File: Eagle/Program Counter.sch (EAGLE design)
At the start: 6 parts, among them J1 55959-2430

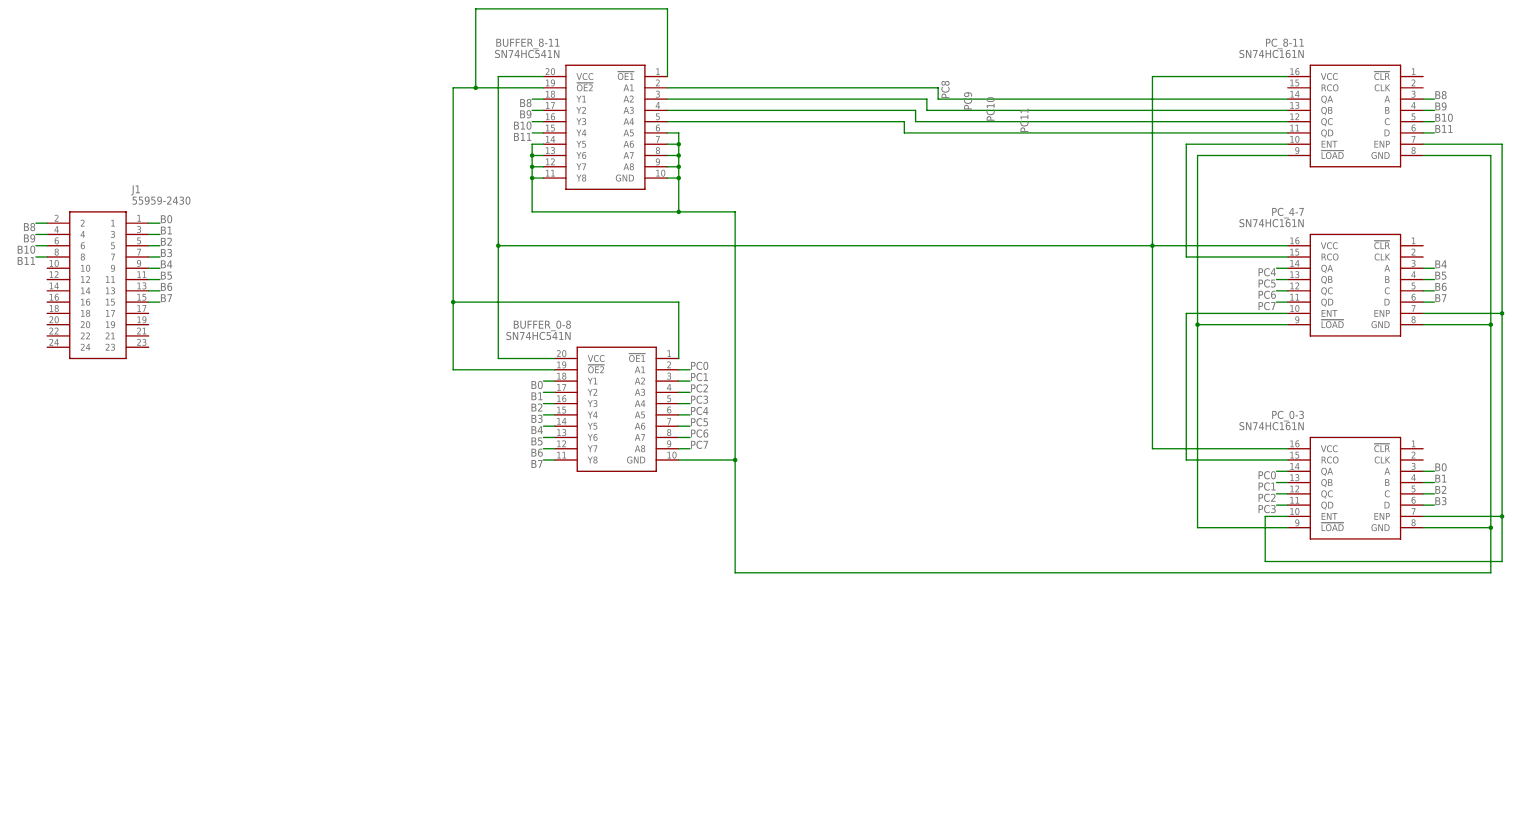
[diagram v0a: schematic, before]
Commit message: finished implementing Program Counter
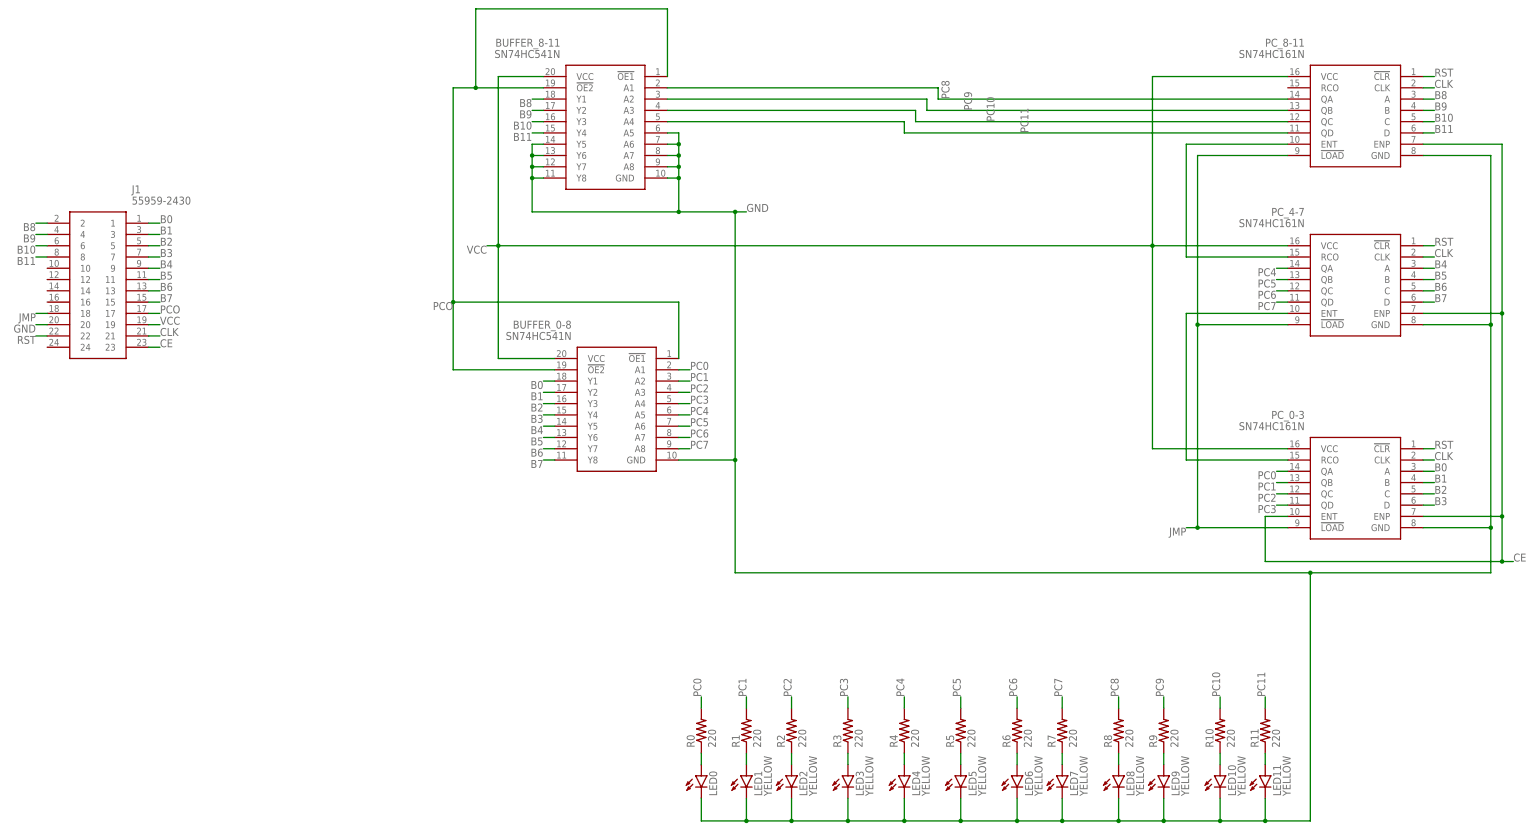
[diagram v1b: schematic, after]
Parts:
- added LED0: (no value), led:LED3MM
- added LED1, LED10, LED11, LED2, LED3, LED4, LED5, LED6, LED7, LED8, LED9: YELLOW, led:LED3MM
- added R0, R1, R10, R11, R2, R3, R4, R5, R6, R7, R8, R9: 220, rcl:R-US_0204/7
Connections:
- removed net N$1: BUFFER_0-8.GND, BUFFER_8-11.A5, BUFFER_8-11.A6, BUFFER_8-11.A7, BUFFER_8-11.A8, BUFFER_8-11.GND, BUFFER_8-11.Y5, BUFFER_8-11.Y6, BUFFER_8-11.Y7, BUFFER_8-11.Y8, PC_0-3.GND, PC_4-7.GND, PC_8-11.GND
- removed net N$4: BUFFER_0-8.!OE1, BUFFER_0-8.!OE2, BUFFER_8-11.!OE1, BUFFER_8-11.!OE2
- removed net N$8: BUFFER_0-8.VCC, BUFFER_8-11.VCC, PC_0-3.VCC, PC_4-7.VCC, PC_8-11.VCC
- new net CE: J1.23, PC_0-3.ENP, PC_0-3.ENT, PC_4-7.ENP, PC_8-11.ENP
- new net CLK: J1.21, PC_0-3.CLK, PC_4-7.CLK, PC_8-11.CLK
- new net GND: BUFFER_0-8.GND, BUFFER_8-11.A5, BUFFER_8-11.A6, BUFFER_8-11.A7, BUFFER_8-11.A8, BUFFER_8-11.GND, BUFFER_8-11.Y5, BUFFER_8-11.Y6, BUFFER_8-11.Y7, BUFFER_8-11.Y8, J1.20, LED0.C, LED1.C, LED10.C, LED11.C, LED2.C, LED3.C, LED4.C, LED5.C, LED6.C, LED7.C, LED8.C, LED9.C, PC_0-3.GND, PC_4-7.GND, PC_8-11.GND
- new net JMP: J1.18, PC_0-3.!LOAD, PC_4-7.!LOAD, PC_8-11.!LOAD
- new net N$10: LED4.A, R4.1
- new net N$11: LED5.A, R5.1
- new net N$12: LED6.A, R6.1
- new net N$13: LED7.A, R7.1
- new net N$14: LED8.A, R8.1
- new net N$15: LED9.A, R9.1
- new net N$16: LED10.A, R10.1
- new net N$17: LED11.A, R11.1
- new net N$7: LED2.A, R2.1
- new net N$9: LED3.A, R3.1
- new net PCO: BUFFER_0-8.!OE1, BUFFER_0-8.!OE2, BUFFER_8-11.!OE1, BUFFER_8-11.!OE2, J1.17
- new net RST: J1.22, PC_0-3.!CLR, PC_4-7.!CLR, PC_8-11.!CLR
- new net VCC: BUFFER_0-8.VCC, BUFFER_8-11.VCC, J1.19, PC_0-3.VCC, PC_4-7.VCC, PC_8-11.VCC
- net N$5: now also LED0.A, R0.1; no longer PC_0-3.!LOAD, PC_4-7.!LOAD, PC_8-11.!LOAD
- net N$6: now also LED1.A, R1.1; no longer PC_0-3.ENP, PC_0-3.ENT, PC_4-7.ENP, PC_8-11.ENP
- net PC0: now also R0.2
- net PC1: now also R1.2
- net PC10: now also R10.2
- net PC11: now also R11.2
- net PC2: now also R2.2
- net PC3: now also R3.2
- net PC4: now also R4.2
- net PC5: now also R5.2
- net PC6: now also R6.2
- net PC7: now also R7.2
- net PC8: now also R8.2
- net PC9: now also R9.2
